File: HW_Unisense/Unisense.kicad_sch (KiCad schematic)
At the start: 63 parts, among them J1 Conn_02x03_Odd_Even, J2 SW1, J3 SW2, J4 GeigerCounter, J5 WS2812, J6 LED1, J7 LED2, J8 LED3, Q1 BSN20, Q2 BSN20, Q3 BSN20, Q4 BSN20, Q5 AO3400A, Q6 AO3400A, Q7 AO3400A, SW1 K2-1102SP-C4SC-04, SW2 K2-1102SP-C4SC-04, SW3 K2-1102SP-C4SC-04, SW4 K2-1102SP-C4SC-04, U1 ESP32-S3-WROOM-1(N8R2), U2 S4B-PH-SM4-K-TB(LF)(SN), U3 LD1117S33TR, U4 TMP112xxDRL, U5 BME280, U6 BMP280, U7 VEML6040A3OG

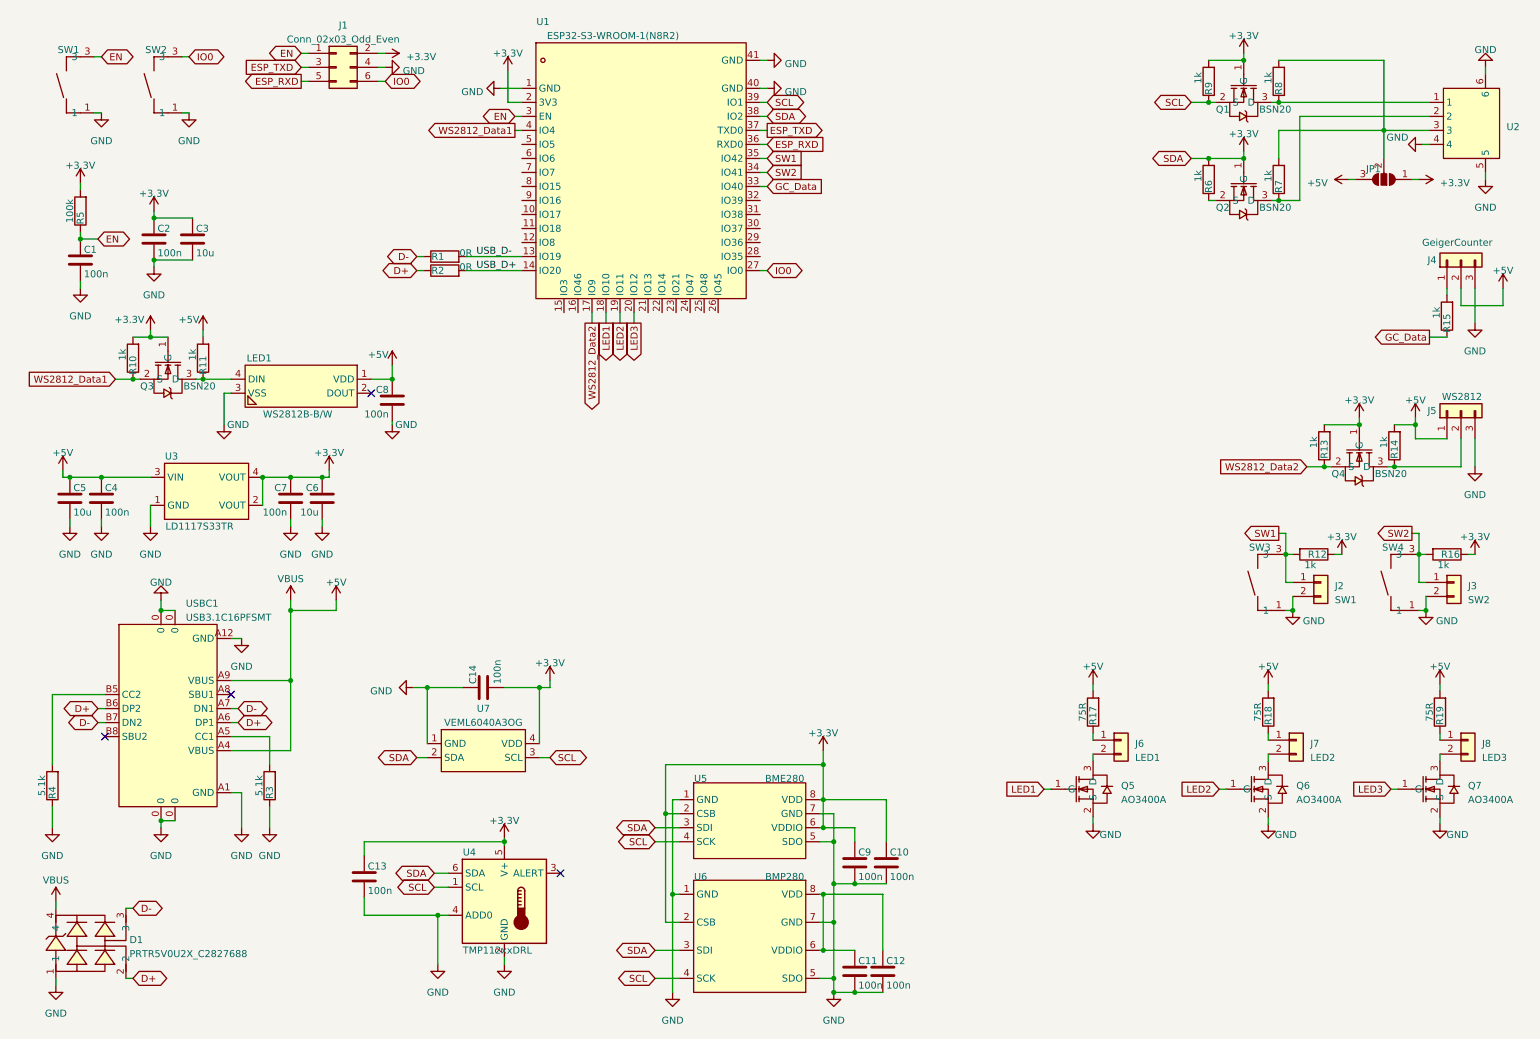
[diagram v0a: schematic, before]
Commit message: add power switching. Add Battery management
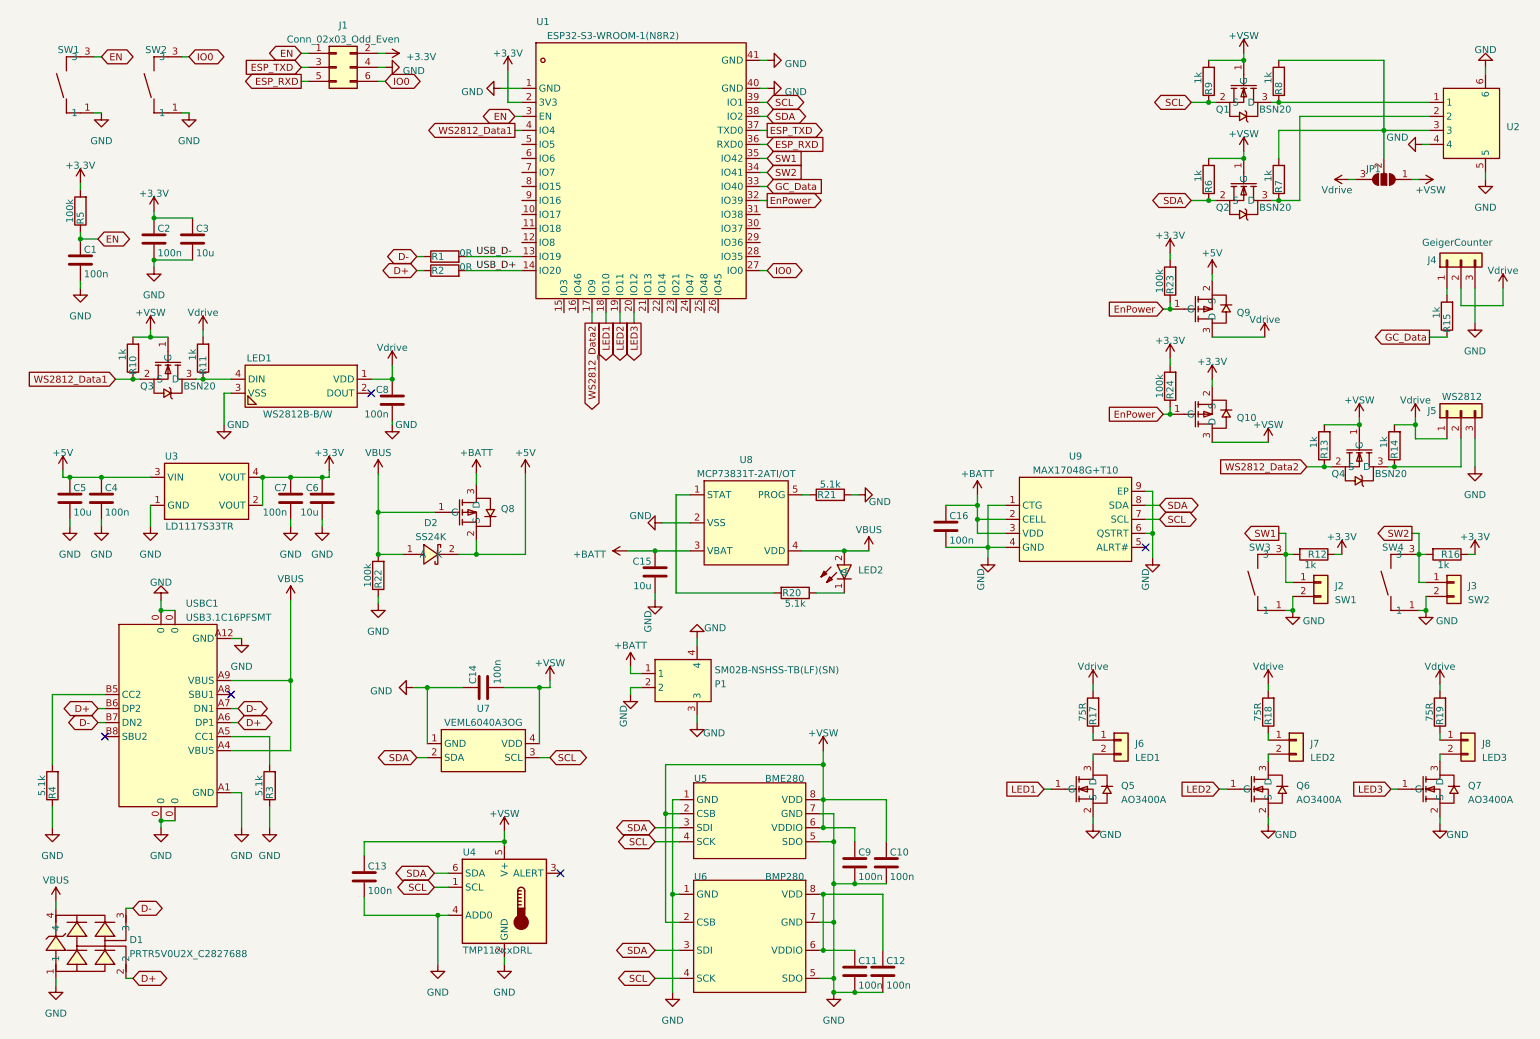
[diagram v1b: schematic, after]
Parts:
- added C15: 10u, Capacitor_SMD:C_0805_2012Metric, symbol Device:C
- added C16: 100n, Capacitor_SMD:C_0603_1608Metric, symbol Device:C
- added D2: SS24K, SMA_L4.3-W2.6-LS5.1-R-RD, symbol burgerLib:SS24K
- added LED2: 19-217/BHC-ZL1M2RY/3T, EduboardV2_kicadlib:LED0603-FD_BLUE, symbol burgerLib:19-217_BHC-ZL1M2RY_3T
- added P1: SM02B-NSHSS-TB(LF)(SN), burgerLibFP:CONN-SMD_SM02B-NSHSS-TB-LF-SN, symbol burgerLib:SM02B-NSHSS-TB(LF)(SN)
- added Q10, Q8, Q9: IRLML6402TRPBF, EduboardV2_kicadlib:SOT-23-3_L2.9-W1.6-P1.90-LS2.8-BR, symbol burgerLib:IRLML6402TRPBF
- added R20, R21: 5.1k, Capacitor_SMD:C_0603_1608Metric, symbol Device:R
- added R22, R23, R24: 100k, Capacitor_SMD:C_0603_1608Metric, symbol Device:R
- added U8: MCP73831T-2ATI/OT, burgerLibFP:SOT-23-5_L3.0-W1.7-P0.95-LS2.8-BR, symbol burgerLib:MCP73831T-2ATI_OT
- added U9: MAX17048G+T10, burgerLibFP:DFN-8_L2.0-W2.0-P0.50-BL-EP, symbol burgerLib:MAX17048G+T10
- C1, C10, C11, C12, C13, C14, C2, C4, C7, C8, C9, R1, R10, R11, R12, R13, R14, R15, R16, R2, R3, R4, R5, R6, R7, R8, R9: footprint (none) -> Capacitor_SMD:C_0603_1608Metric
- C3, C5, C6, R17, R18, R19: footprint (none) -> Capacitor_SMD:C_0805_2012Metric
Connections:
- net +3.3V: now also Q10.2 (S), R23.2, R24.2; no longer C10.1, C13.1, C14.2, C9.1, JP1.1 (A), Q1.1 (G), Q2.1 (G), Q3.1 (G), Q4.1 (G), R10.2, R13.2, R6.2, R9.2, U1.38 (IO2), U4.5 (V+), U4.6 (SDA), U5.2 (CSB), U5.3 (SDI), U5.6 (VDDIO), U5.8 (VDD), U6.2 (CSB), U6.3 (SDI), U7.2 (SDA), U7.4 (VDD)
- net +5V: now also D2.2 (K), Q8.2 (S), Q9.2 (S); no longer C8.1, D1.4, J4.2 (Pin_2), J5.1 (Pin_1), JP1.3 (B), LED1.1 (VDD), R11.2, R14.2, R17.2, R18.2, R19.2, USBC1.A4 (VBUS), USBC1.A9 (VBUS)
- net GND: now also C15.2, C16.2, P1.2, P1.3, P1.4, R21.2, R22.1, U8.2 (VSS), U9.1 (CTG), U9.4 (GND), U9.6 (QSTRT), U9.9 (EP)
- net SCL: now also U9.7 (SCL)
- net SDA: now reaches Q2.2 (S), R6.1
- net SDA: now also U1.38 (IO2), U4.6 (SDA), U5.3 (SDI), U6.3 (SDI), U7.2 (SDA), U9.8 (SDA)
- net EnPower: now reaches U1.32 (IO39)
- net EnPower: now also Q10.1 (G), Q9.1 (G), R23.1, R24.1
- new net: LED2.1 (C), R20.1
- new net: R20.2, U8.1 (STAT)
- new net: R21.1, U8.5 (PROG)
- new net +BATT: C15.1, C16.1, P1.1, Q8.3 (D), U8.3 (VBAT), U9.2 (CELL), U9.3 (VDD)
- new net +VSW: C10.1, C13.1, C14.2, C9.1, JP1.1 (A), Q1.1 (G), Q10.3 (D), Q2.1 (G), Q3.1 (G), Q4.1 (G), R10.2, R13.2, R6.2, R9.2, U4.5 (V+), U5.2 (CSB), U5.6 (VDDIO), U5.8 (VDD), U6.2 (CSB), U7.4 (VDD)
- new net VBUS: D1.4, D2.1 (A), LED2.2 (A), Q8.1 (G), R22.2, U8.4 (VDD), USBC1.A4 (VBUS), USBC1.A9 (VBUS)
- new net Vdrive: C8.1, J4.2 (Pin_2), J5.1 (Pin_1), JP1.3 (B), LED1.1 (VDD), Q9.3 (D), R11.2, R14.2, R17.2, R18.2, R19.2
- no-connect marks 4 -> 5

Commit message: add more sensors and arrange on multiple pages
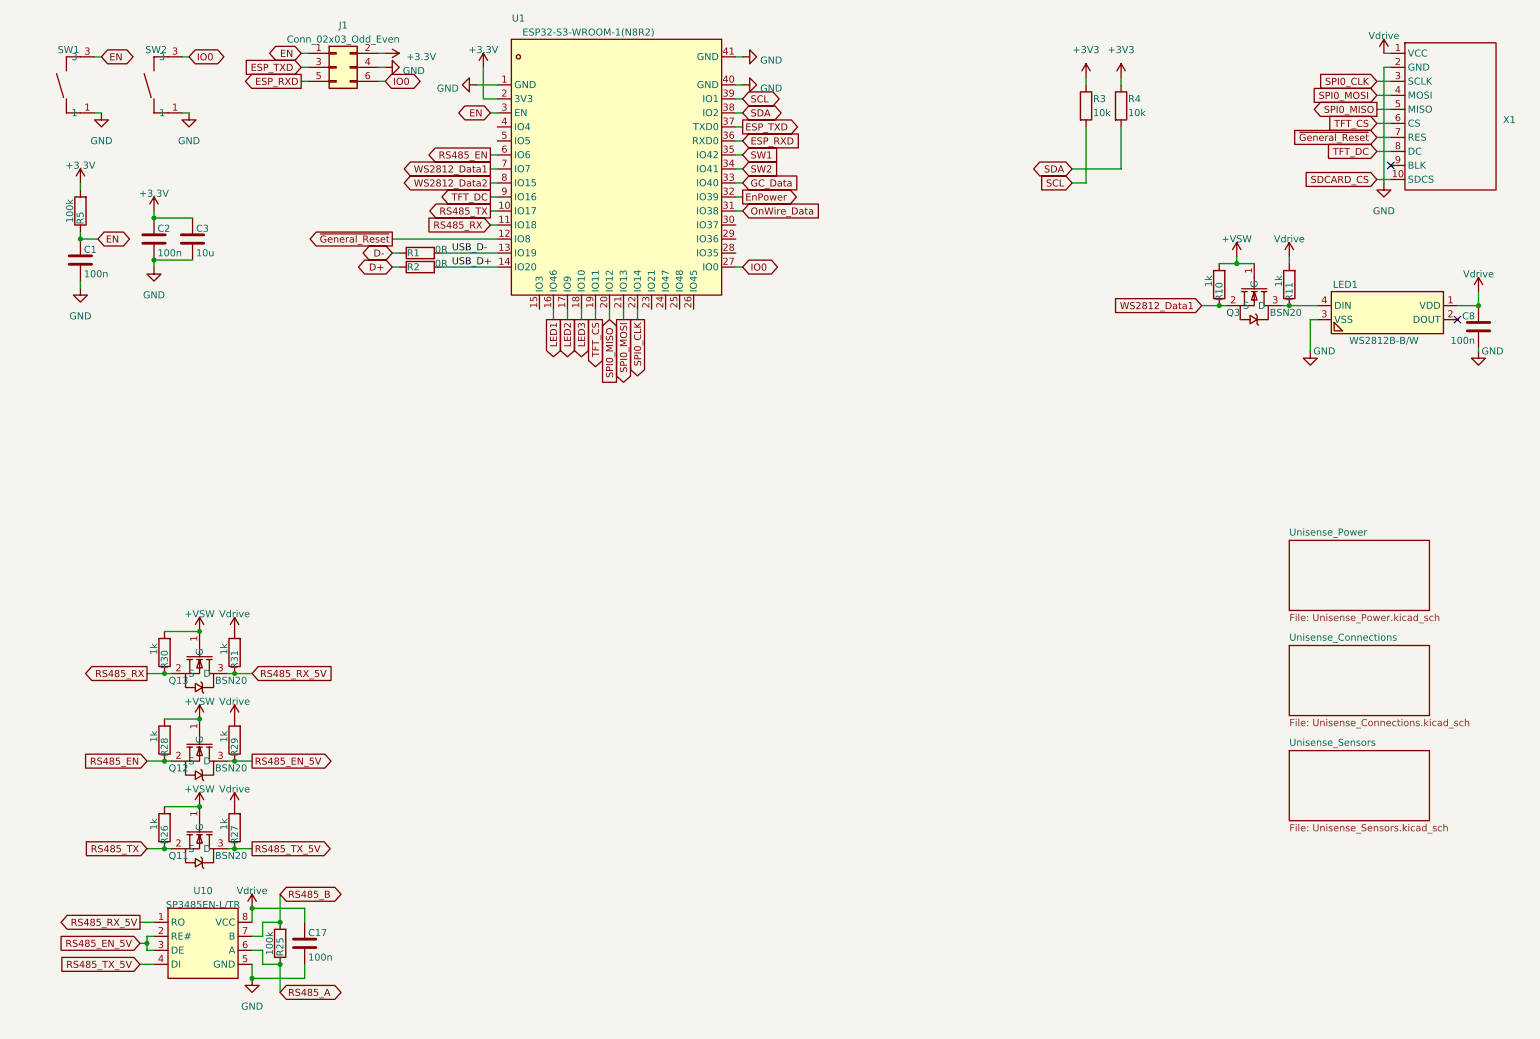
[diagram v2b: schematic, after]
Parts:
- removed C10, C11, C12, C13, C14, C16, C4, C7, C9: 100n, Capacitor_SMD:C_0603_1608Metric, symbol Device:C
- removed C15, C5, C6: 10u, Capacitor_SMD:C_0805_2012Metric, symbol Device:C
- removed D1: PRTR5V0U2X_C2827688, EduboardV2_kicadlib:SOT-143-4_L2.9-W1.3-P1.92-LS2.4-BL, symbol burgerLib:PRTR5V0U2X_C2827688
- removed D2: SS24K, SMA_L4.3-W2.6-LS5.1-R-RD, symbol burgerLib:SS24K
- removed J2: SW1, Connector_PinHeader_2.54mm:PinHeader_1x02_P2.54mm_Vertical, symbol Connector_Generic:Conn_01x02
- removed J3: SW2, Connector_PinHeader_2.54mm:PinHeader_1x02_P2.54mm_Vertical, symbol Connector_Generic:Conn_01x02
- removed J4: GeigerCounter, Connector_PinHeader_2.54mm:PinHeader_1x03_P2.54mm_Vertical, symbol Connector_Generic:Conn_01x03
- removed J5: WS2812, Connector_PinHeader_2.54mm:PinHeader_1x03_P2.54mm_Vertical, symbol Connector_Generic:Conn_01x03
- removed J6: LED1, Connector_PinHeader_2.54mm:PinHeader_1x02_P2.54mm_Vertical, symbol Connector_Generic:Conn_01x02
- removed J7: LED2, Connector_PinHeader_2.54mm:PinHeader_1x02_P2.54mm_Vertical, symbol Connector_Generic:Conn_01x02
- removed J8: LED3, Connector_PinHeader_2.54mm:PinHeader_1x02_P2.54mm_Vertical, symbol Connector_Generic:Conn_01x02
- removed JP1: SolderJumper_3_Open, symbol Jumper:SolderJumper_3_Open
- removed LED2: 19-217/BHC-ZL1M2RY/3T, EduboardV2_kicadlib:LED0603-FD_BLUE, symbol burgerLib:19-217_BHC-ZL1M2RY_3T
- removed P1: SM02B-NSHSS-TB(LF)(SN), burgerLibFP:CONN-SMD_SM02B-NSHSS-TB-LF-SN, symbol burgerLib:SM02B-NSHSS-TB(LF)(SN)
- removed Q1, Q2, Q4: BSN20, EduboardV2_kicadlib:SOT-23-3_L2.9-W1.6-P1.90-LS2.8-BR, symbol burgerLib:BSN20
- removed Q10, Q8, Q9: IRLML6402TRPBF, EduboardV2_kicadlib:SOT-23-3_L2.9-W1.6-P1.90-LS2.8-BR, symbol burgerLib:IRLML6402TRPBF
- removed Q5, Q6, Q7: AO3400A, EduboardV2_kicadlib:SOT-23-3_L2.9-W1.6-P1.90-LS2.8-BR, symbol burgerLib:AO3400A
- removed R12, R13, R14, R15, R16, R6, R7, R8, R9: 1k, Capacitor_SMD:C_0603_1608Metric, symbol Device:R
- removed R17, R18, R19: 75R, Capacitor_SMD:C_0805_2012Metric, symbol Device:R
- removed R20, R21: 5.1k, Capacitor_SMD:C_0603_1608Metric, symbol Device:R
- removed R22, R23, R24: 100k, Capacitor_SMD:C_0603_1608Metric, symbol Device:R
- removed SW3, SW4: K2-1102SP-C4SC-04, EduboardV2_kicadlib:KEY-SMD_4P-L6.0-W6.0-P4.50-LS9.5-BL, symbol burgerLib:K2-1102SP-C4SC-04
- removed U2: S4B-PH-SM4-K-TB(LF)(SN), EduboardV2_kicadlib:CONN-SMD_S4B-PH-SM4-K-TB-LF-SN, symbol burgerLib:S4B-PH-SM4-K-TB(LF)(SN)
- removed U3: LD1117S33TR, EduboardV2_kicadlib:SOT-223_L6.5-W3.5-P2.30-LS7.0-BR, symbol burgerLib:LD1117S33TR
- removed U4: TMP112xxDRL, Package_TO_SOT_SMD:SOT-563, symbol Sensor_Temperature:TMP112xxDRL
- removed U5: BME280, burgerLibFP:LGA-8_BME280_BL, symbol burgerLib:BME280
- removed U6: BMP280, burgerLibFP:LGA-8_L2.5-W2.0-P0.65_AMP6127, symbol burgerLib:BMP280
- removed U7: VEML6040A3OG, burgerLibFP:SENSOR_SMD_VEML6040A3OG, symbol burgerLib:VEML6040A3OG
- removed U8: MCP73831T-2ATI/OT, burgerLibFP:SOT-23-5_L3.0-W1.7-P0.95-LS2.8-BR, symbol burgerLib:MCP73831T-2ATI_OT
- removed U9: MAX17048G+T10, burgerLibFP:DFN-8_L2.0-W2.0-P0.50-BL-EP, symbol burgerLib:MAX17048G+T10
- removed USBC1: USB3.1C16PFSMT, EduboardV2_kicadlib:USB-C-SMD_TYPE-C-USB-17, symbol burgerLib:USB3.1C16PFSMT
- added C17: 100n, Capacitor_SMD:C_0603_1608Metric, symbol Device:C
- added Q11, Q12, Q13: BSN20, EduboardV2_kicadlib:SOT-23-3_L2.9-W1.6-P1.90-LS2.8-BR, symbol burgerLib:BSN20
- added R25: 100k, Resistor_SMD:R_0603_1608Metric_Pad0.98x0.95mm_HandSolder, symbol Device:R
- added R26, R27, R28, R29, R30, R31: 1k, Resistor_SMD:R_0603_1608Metric_Pad0.98x0.95mm_HandSolder, symbol Device:R
- added U10: SP3485EN-L/TR, EduboardV2_kicadlib:SOIC-8_L5.0-W4.0-P1.27-LS6.0-BL, symbol burgerLib:SP3485EN-L_TR
- added X1: ~, burgerLibFP:DFR0649, symbol burgerLib:DFR0649
- R1, R2: footprint Capacitor_SMD:C_0603_1608Metric -> Resistor_SMD:R_0805_2012Metric_Pad1.20x1.40mm_HandSolder
- R10, R11, R5: footprint Capacitor_SMD:C_0603_1608Metric -> Resistor_SMD:R_0603_1608Metric_Pad0.98x0.95mm_HandSolder
- R3, R4: value 5.1k -> 10k; footprint Capacitor_SMD:C_0603_1608Metric -> Resistor_SMD:R_0805_2012Metric; LCSC Part # (none) -> C17414
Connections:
- net +VSW: now also Q11.1 (G), Q12.1 (G), Q13.1 (G), R26.2, R28.2, R30.2
- net GND: now also C17.2, U10.5 (GND), X1.2 (GND); no longer R3.1, R4.1
- net LED1: now also U1.16 (IO46); no longer U1.18 (IO10)
- net LED2: now also U1.17 (IO9); no longer U1.19 (IO11)
- net LED3: now also U1.18 (IO10); no longer U1.20 (IO12)
- net SCL: now also R3.2
- net SDA: now also R4.2
- net Vdrive: now also C17.1, R27.2, R29.2, R31.2, U10.8 (VCC), X1.1 (VCC)
- net WS2812_Data1: now also U1.7 (IO7); no longer U1.4 (IO4)
- net WS2812_Data2: now also U1.8 (IO15); no longer U1.17 (IO9)
- net RS485_TX: now reaches U1.10 (IO17)
- net RS485_TX: now also Q11.2 (S), R26.1
- net RS485_RX: now reaches U1.11 (IO18)
- net RS485_RX: now also Q13.2 (S), R30.1
- net ~{General_Reset}: now reaches U1.12 (IO8)
- net ~{General_Reset}: now also X1.7 (RES)
- net SPI0_MOSI: now reaches U1.21 (IO13)
- net SPI0_MOSI: now also X1.4 (MOSI)
- net SPI0_CLK: now reaches U1.22 (IO14)
- net SPI0_CLK: now also X1.3 (SCLK)
- net OnWire_Data: now reaches U1.31 (IO38)
- net RS485_EN: now reaches U1.6 (IO6)
- net RS485_EN: now also Q12.2 (S), R28.1
- net TFT_DC: now reaches U1.9 (IO16)
- net TFT_DC: now also X1.8 (DC)
- new net +3V3: R3.1, R4.1
- new net RS485_A: R25.1, U10.6 (A)
- new net RS485_B: R25.2, U10.7 (B)
- new net RS485_EN_5V: Q12.3 (D), R29.1, U10.2 (RE#), U10.3 (DE)
- new net RS485_RX_5V: Q13.3 (D), R31.1, U10.1 (RO)
- new net RS485_TX_5V: Q11.3 (D), R27.1, U10.4 (DI)
- new net SDCARD_CS: X1.10 (SDCS)
- new net SPI0_MISO: U1.20 (IO12), X1.5 (MISO)
- new net TFT_CS: U1.19 (IO11), X1.6 (CS)
- no-connect marks 5 -> 2
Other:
- added sheet Unisense_Connections (Unisense_Connections.kicad_sch)
- added sheet Unisense_Power (Unisense_Power.kicad_sch)
- added sheet Unisense_Sensors (Unisense_Sensors.kicad_sch)
- moved on the sheet: C8, LED1, Q3, R1, R10, R11, R2, U1

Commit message: change power net names, as V8 handles them like a champ
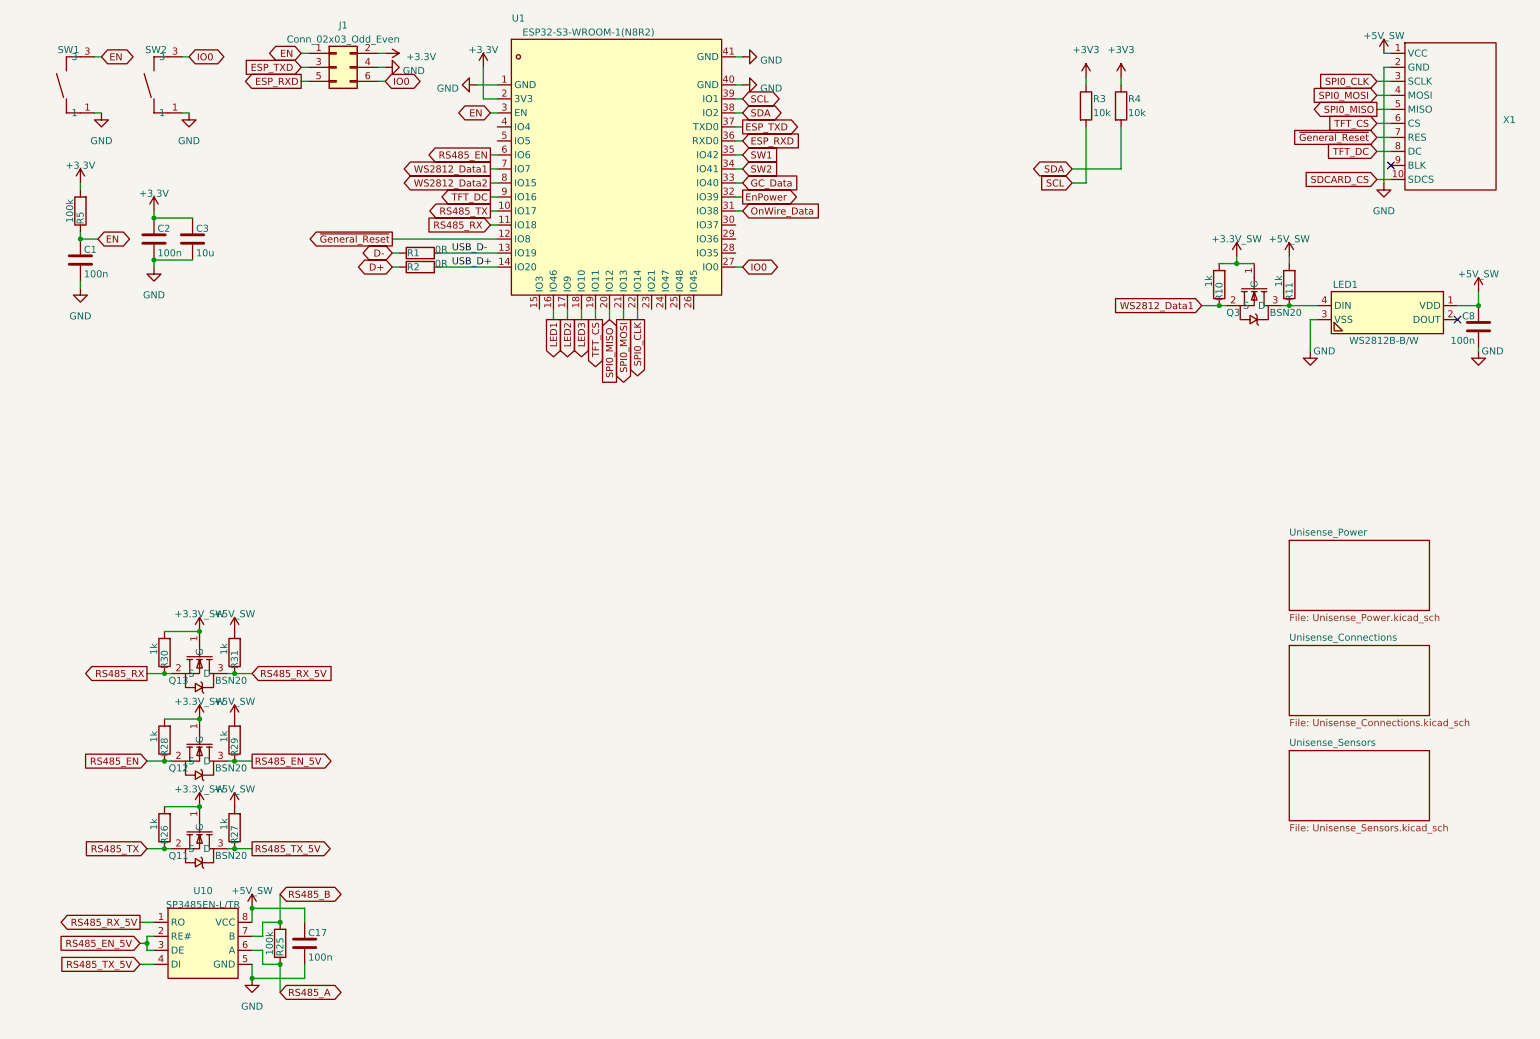
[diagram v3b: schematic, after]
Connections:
- net +VSW renamed +3.3V_SW
- net Vdrive renamed +5V_SW

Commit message: add mor sensors, place parts
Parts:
- J1: footprint (none) -> Connector_PinHeader_2.54mm:PinHeader_2x03_P2.54mm_Vertical
- R3, R4: footprint Resistor_SMD:R_0805_2012Metric -> Resistor_SMD:R_0603_1608Metric_Pad0.98x0.95mm_HandSolder
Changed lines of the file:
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@@
 			)
 		)
-		(property "Footprint" "Resistor_SMD:R_0805_2012Metric"
+		(property "Footprint" "Resistor_SMD:R_0603_1608Metric_Pad0.98x0.95mm_HandSolder"
 			(at 209.042 29.21 90)
 			(effects
@@
 			)
 		)
-		(property "Footprint" ""
+		(property "Footprint" "Connector_PinHeader_2.54mm:PinHeader_2x03_P2.54mm_Vertical"
 			(at 68.58 22.225 0)
 			(effects
@@
 			)
 		)
-		(property "Footprint" "Resistor_SMD:R_0805_2012Metric"
+		(property "Footprint" "Resistor_SMD:R_0603_1608Metric_Pad0.98x0.95mm_HandSolder"
 			(at 202.692 29.21 90)
 			(effects
